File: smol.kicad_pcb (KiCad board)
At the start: 2 copper layers, 141 parts, among them SW1 keyswitch, SW10 keyswitch, SW11 keyswitch, SW12 keyswitch, SW13 keyswitch, SW14 keyswitch, SW15 keyswitch, SW16 keyswitch, SW17 keyswitch, SW18 keyswitch, SW19 keyswitch, SW2 keyswitch, SW20 keyswitch, SW21 keyswitch, SW22 keyswitch, SW23 keyswitch, SW24 keyswitch, SW25 keyswitch, SW26 keyswitch, SW27 keyswitch, SW28 keyswitch, SW29 keyswitch, SW3 keyswitch, SW30 keyswitch, SW31 keyswitch, SW32 keyswitch, SW33 keyswitch, SW34 keyswitch, SW35 keyswitch, SW36 keyswitch, SW37 keyswitch, SW38 keyswitch, SW39 keyswitch, SW4 keyswitch, SW40 keyswitch, SW41 keyswitch, SW42 keyswitch, SW43 keyswitch, SW44 keyswitch, SW45 keyswitch, SW46 keyswitch, SW47 keyswitch, SW48 keyswitch, SW49 keyswitch, SW5 keyswitch, SW50 keyswitch, SW51 keyswitch, SW52 keyswitch, SW53 keyswitch, SW54 keyswitch, SW55 keyswitch, SW56 keyswitch, SW57 keyswitch, SW58 keyswitch, SW59 keyswitch, SW6 keyswitch, SW60 keyswitch, SW61 keyswitch, SW62 keyswitch, SW63 keyswitch, SW64 keyswitch, SW65 keyswitch, SW66 keyswitch, SW67 keyswitch, SW68 keyswitch, SW69 keyswitch, SW7 keyswitch, SW70 keyswitch, SW8 keyswitch, SW9 keyswitch, U1 MiniF4x1Cx_V31

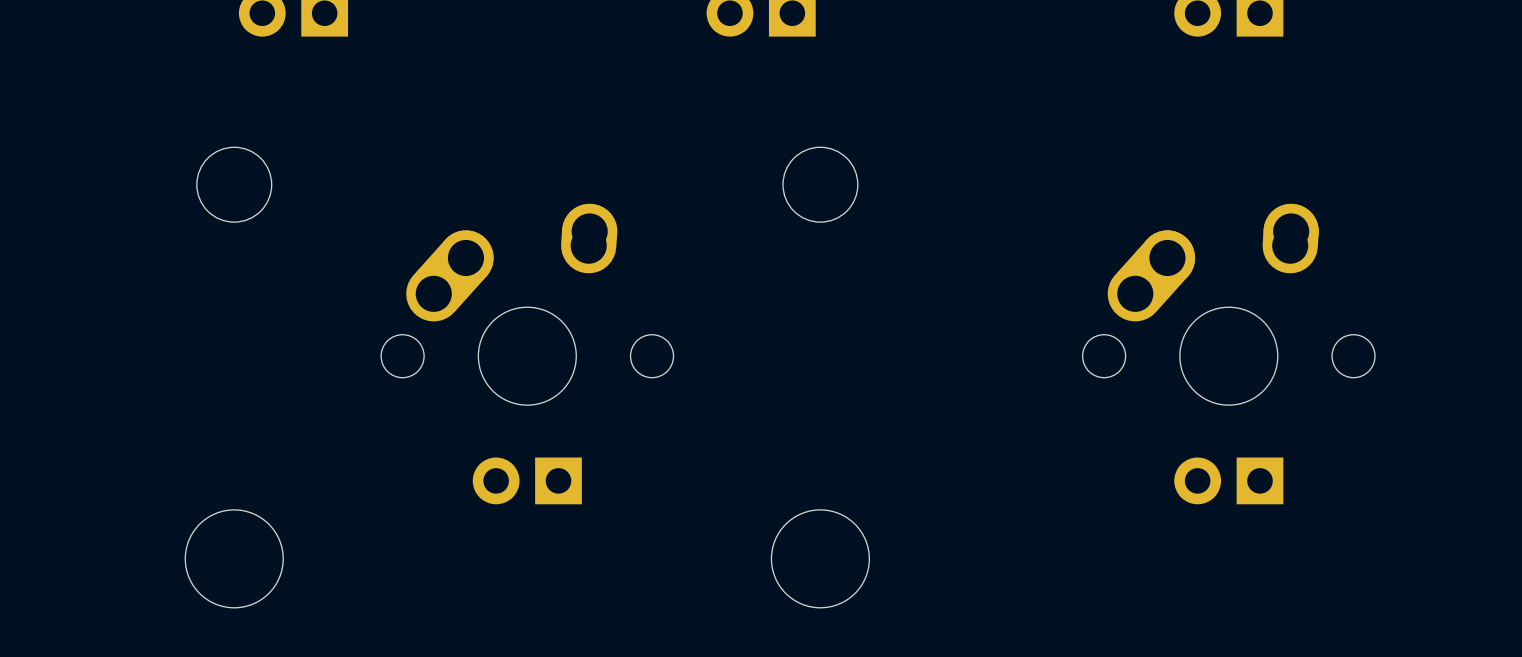
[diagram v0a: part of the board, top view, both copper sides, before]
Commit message: move space bar one key to the right
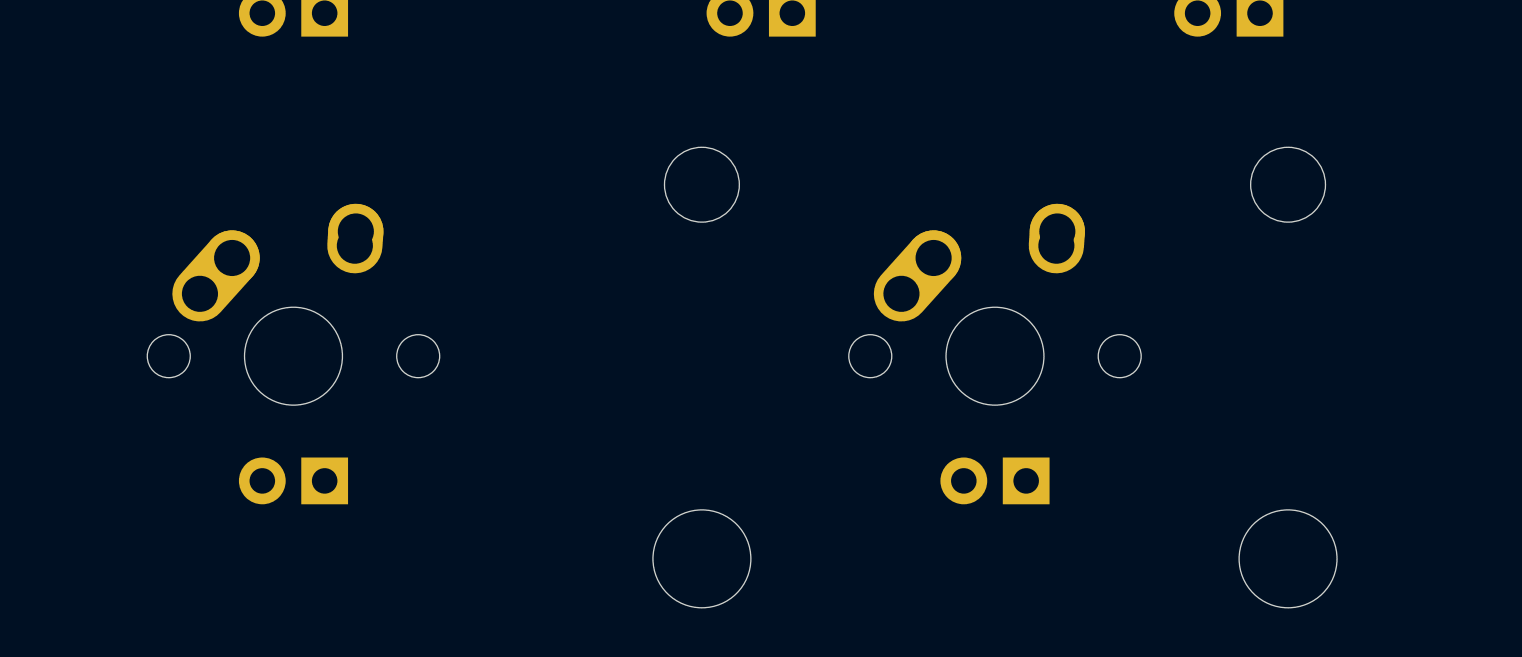
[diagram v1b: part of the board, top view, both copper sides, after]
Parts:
- SW62: footprint MX_Alps_Hybrid:MX-2U -> MX_Alps_Hybrid:MX-1U
- SW63: footprint MX_Alps_Hybrid:MX-1U -> MX_Alps_Hybrid:MX-2U
- moved SW62 9.53 mm to (110.3, 99.2)
- moved SW63 9.53 mm to (138.9, 99.2)

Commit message: position diodes on pcb
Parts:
- D1, D10, D11, D12, D13, D14, D15, D16, D17, D18, D19, D2, D20, D21, D22, D23, D24, D25, D26, D27, D28, D29, D3, D30, D31, D32, D33, D34, D35, D36, D37, D38, D39, D4, D40, D41, D42, D43, D44, D45, D46, D47, D48, D49, D5, D50, D51, D52, D53, D54, D55, D56, D57, D58, D59, D6, D60, D61, D62, D63, D64, D65, D66, D67, D68, D69, D7, D70, D8, D9: moved to B.Cu
- moved D15 436.7 mm to (22.2, 50.0), turned to 270 degrees
- moved D16 404.2 mm to (50.8, 50.0), turned to 270 degrees
- moved D57 387.4 mm to (12.7, 107.2), turned to 270 degrees
- moved D30 384.3 mm to (31.8, 69.1), turned to 270 degrees
- moved D32 381.1 mm to (69.8, 69.1), turned to 270 degrees
- moved D43 380.6 mm to (22.2, 88.1), turned to 270 degrees
- moved D1 370.5 mm to (12.7, 31.0), turned to 270 degrees
- moved D44 366.1 mm to (50.8, 88.1), turned to 270 degrees
- moved D58 365.4 mm to (31.8, 107.2), turned to 270 degrees
- moved D46 346.5 mm to (88.9, 88.1), turned to 270 degrees
- moved D59 343.6 mm to (50.8, 107.2), turned to 270 degrees
- moved D34 340.0 mm to (108.0, 69.1), turned to 270 degrees
- moved D47 324.4 mm to (108.0, 88.1), turned to 270 degrees
- moved D33 324.2 mm to (88.9, 69.1), turned to 270 degrees
- moved D60 322.1 mm to (69.8, 107.2), turned to 270 degrees
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
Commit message: switch to mx switch footprints and line up diodes
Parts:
- SW1, SW10, SW11, SW12, SW13, SW16, SW17, SW18, SW19, SW2, SW20, SW21, SW22, SW23, SW24, SW25, SW26, SW27, SW28, SW29, SW3, SW30, SW31, SW32, SW33, SW34, SW35, SW36, SW37, SW38, SW39, SW4, SW40, SW41, SW44, SW45, SW46, SW47, SW48, SW49, SW5, SW50, SW51, SW52, SW53, SW54, SW55, SW56, SW57, SW58, SW59, SW6, SW60, SW61, SW62, SW64, SW65, SW66, SW67, SW68, SW69, SW7, SW70, SW8, SW9: value keyswitch -> 1U; footprint MX_Alps_Hybrid:MX-1U -> MX_Only:MXOnly-1U-NoLED
- SW14, SW15, SW42, SW43, SW63: value keyswitch -> 2U; footprint MX_Alps_Hybrid:MX-2U -> MX_Only:MXOnly-2U-NoLED
- moved D11 4.63 mm to (205.6, 27.0), turned to 0 degrees
- moved D14 4.63 mm to (272.3, 27.0), turned to 0 degrees
- moved D24 4.63 mm to (205.6, 46.0), turned to 0 degrees
- moved D28 4.63 mm to (281.8, 46.0), turned to 0 degrees
- moved D39 4.63 mm to (205.6, 65.1), turned to 0 degrees
- moved D42 4.63 mm to (272.3, 65.1), turned to 0 degrees
- moved D52 4.63 mm to (205.6, 84.1), turned to 0 degrees
- moved D56 4.63 mm to (281.8, 84.1), turned to 0 degrees
- moved D66 4.63 mm to (205.6, 103.2), turned to 0 degrees
- moved D70 4.63 mm to (281.8, 103.2), turned to 0 degrees
- moved D17 4.63 mm to (72.2, 46.0), turned to 0 degrees
- moved D32 4.63 mm to (72.2, 65.1), turned to 0 degrees
- moved D4 4.63 mm to (72.2, 27.0), turned to 0 degrees
- moved D45 4.63 mm to (72.2, 84.1), turned to 0 degrees
- moved D60 4.63 mm to (72.2, 103.2), turned to 0 degrees
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
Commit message: connect matrix to blackpill
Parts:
- moved U1 412.2 mm to (-11.9, -15.9)
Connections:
- U1 pad 1: Net-(U1-Pad1) -> ROW5
- U1 pad 10: Net-(U1-Pad10) -> COL2
- U1 pad 11: Net-(U1-Pad11) -> COL3
- U1 pad 12: Net-(U1-Pad12) -> COL4
- U1 pad 13: Net-(U1-Pad13) -> COL5
- U1 pad 14: Net-(U1-Pad14) -> COL6
- U1 pad 15: Net-(U1-Pad15) -> COL7
- U1 pad 16: Net-(U1-Pad16) -> COL8
- U1 pad 17: Net-(U1-Pad17) -> COL9
- U1 pad 2: Net-(U1-Pad2) -> ROW4
- U1 pad 3: Net-(U1-Pad3) -> ROW3
- U1 pad 32: Net-(U1-Pad32) -> COL14
- U1 pad 33: Net-(U1-Pad33) -> COL13
- U1 pad 34: Net-(U1-Pad34) -> COL12
- U1 pad 35: Net-(U1-Pad35) -> COL11
- U1 pad 37: Net-(U1-Pad37) -> COL10
- U1 pad 4: Net-(U1-Pad4) -> ROW2
- U1 pad 5: Net-(U1-Pad5) -> ROW1
- U1 pad 7: Net-(U1-Pad7) -> COL1

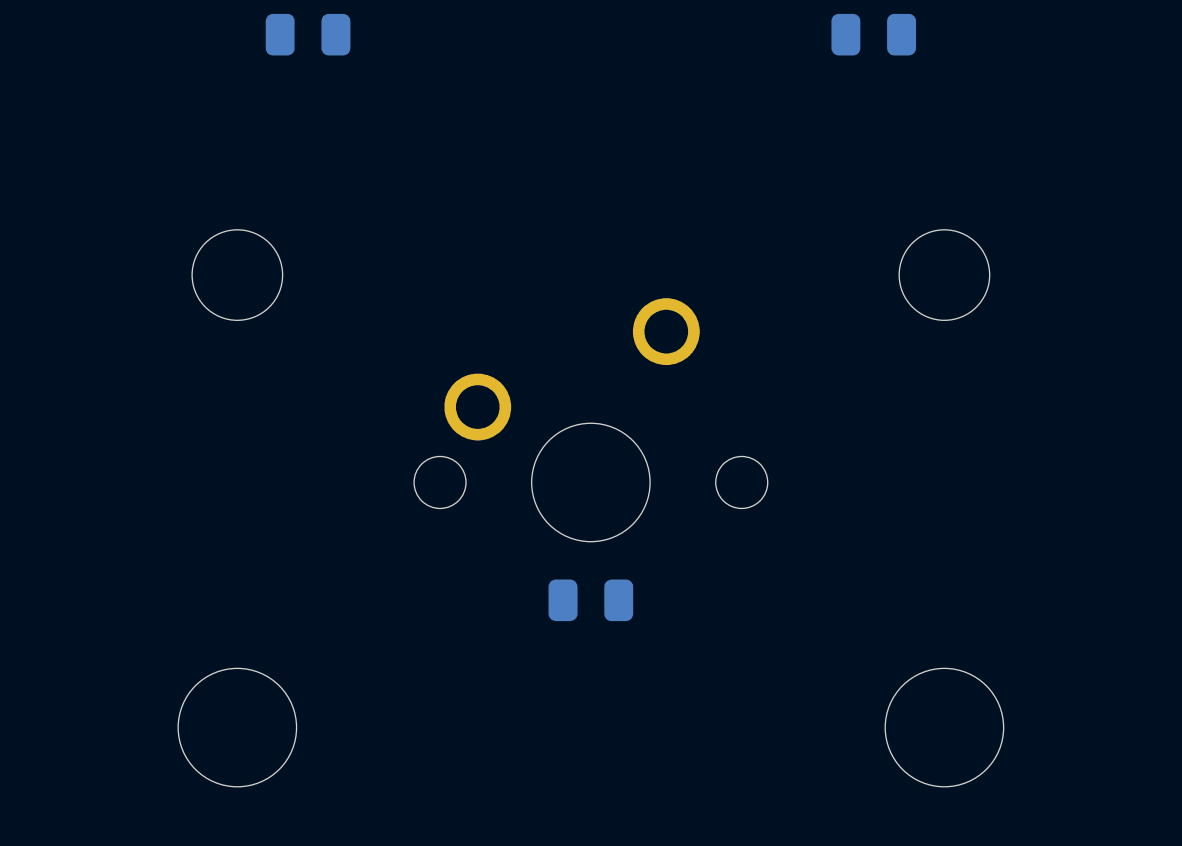
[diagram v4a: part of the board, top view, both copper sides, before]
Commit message: use inverted stab on bottow row
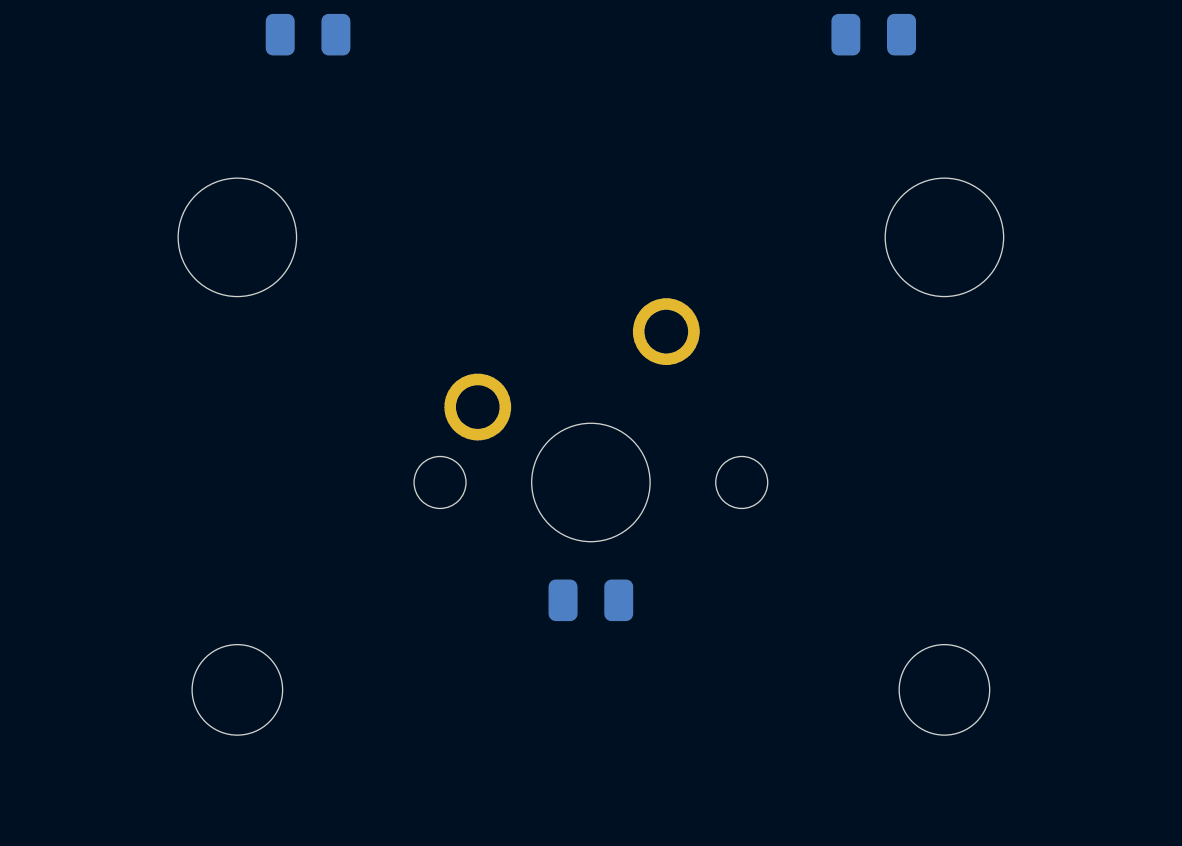
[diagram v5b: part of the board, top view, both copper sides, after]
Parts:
- SW63: footprint MX_Only:MXOnly-2U-NoLED -> MX_Only:MXOnly-2U-ReversedStabilizers-NoLED

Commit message: add leds to pcb
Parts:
- added C1: 100nf, Capacitor_SMD:C_0805_2012Metric, F.Cu at (-3.97, 23.0)
- added C10: 100nf, Capacitor_SMD:C_0805_2012Metric, F.Cu at (300.8, 23.0)
- added C2: 100nf, Capacitor_SMD:C_0805_2012Metric, F.Cu at (-3.97, 42.1)
- added C3: 100nf, Capacitor_SMD:C_0805_2012Metric, F.Cu at (-3.97, 61.1)
- added C4: 100nf, Capacitor_SMD:C_0805_2012Metric, F.Cu at (-3.97, 80.2)
- added C5: 100nf, Capacitor_SMD:C_0805_2012Metric, F.Cu at (-3.97, 99.2)
- added C6: 100nf, Capacitor_SMD:C_0805_2012Metric, F.Cu at (300.8, 99.2)
- added C7: 100nf, Capacitor_SMD:C_0805_2012Metric, F.Cu at (300.8, 80.2)
- added C8: 100nf, Capacitor_SMD:C_0805_2012Metric, F.Cu at (300.8, 61.1)
- added C9: 100nf, Capacitor_SMD:C_0805_2012Metric, F.Cu at (300.8, 42.1)
- added Q1: BSS138, Package_TO_SOT_SMD:SOT-23, F.Cu at (-10.3, -34.1)
- added R1: 10k, Resistor_SMD:R_0805_2012Metric, F.Cu at (-34.9, -34.1)
- added R2: 10k, Resistor_SMD:R_0805_2012Metric, F.Cu at (-26.2, -32.5)
- added RGB1: SK6812, LED_SMD:LED_SK6812_PLCC4_5.0x5.0mm_P3.2mm, F.Cu at (0.79, 23.0)
- added RGB10: SK6812, LED_SMD:LED_SK6812_PLCC4_5.0x5.0mm_P3.2mm, F.Cu at (296.1, 23.0)
- added RGB2: SK6812, LED_SMD:LED_SK6812_PLCC4_5.0x5.0mm_P3.2mm, F.Cu at (0.79, 42.1)
- added RGB3: SK6812, LED_SMD:LED_SK6812_PLCC4_5.0x5.0mm_P3.2mm, F.Cu at (0.79, 61.1)
- added RGB4: SK6812, LED_SMD:LED_SK6812_PLCC4_5.0x5.0mm_P3.2mm, F.Cu at (0.79, 80.2)
- added RGB5: SK6812, LED_SMD:LED_SK6812_PLCC4_5.0x5.0mm_P3.2mm, F.Cu at (0.79, 99.2)
- added RGB6: SK6812, LED_SMD:LED_SK6812_PLCC4_5.0x5.0mm_P3.2mm, F.Cu at (296.1, 99.2)
- added RGB7: SK6812, LED_SMD:LED_SK6812_PLCC4_5.0x5.0mm_P3.2mm, F.Cu at (296.1, 80.2)
- added RGB8: SK6812, LED_SMD:LED_SK6812_PLCC4_5.0x5.0mm_P3.2mm, F.Cu at (296.1, 61.1)
- added RGB9: SK6812, LED_SMD:LED_SK6812_PLCC4_5.0x5.0mm_P3.2mm, F.Cu at (296.1, 42.1)
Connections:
- net VCC renamed +3V3
- U1 pad 18: Net-(U1-Pad18) -> +5V
- U1 pad 31: Net-(U1-Pad31) -> COL14
- U1 pad 32: COL14 -> COL13
- U1 pad 33: COL13 -> COL12
- U1 pad 34: COL12 -> COL11
- U1 pad 35: COL11 -> COL10
- U1 pad 37: COL10 -> RGB
- U1 pad 40: Net-(U1-Pad40) -> +5V

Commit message: reorganize for easier routing
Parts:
- moved C1 304.8 mm to (300.8, 23.0)
- moved C10 304.8 mm to (-3.97, 23.0)
- moved C2 304.8 mm to (300.8, 42.1)
- moved C3 304.8 mm to (300.8, 61.1)
- moved C4 304.8 mm to (300.8, 80.2)
- moved C5 304.8 mm to (300.8, 99.2)
- moved C6 304.8 mm to (-3.97, 99.2)
- moved C7 304.8 mm to (-3.97, 80.2)
- moved C8 304.8 mm to (-3.97, 61.1)
- moved C9 304.8 mm to (-3.97, 42.1)
- moved RGB1 295.3 mm to (296.1, 23.0)
- moved RGB10 295.3 mm to (0.79, 23.0)
- moved RGB2 295.3 mm to (296.1, 42.1)
- moved RGB3 295.3 mm to (296.1, 61.1)
- moved RGB4 295.3 mm to (296.1, 80.2)
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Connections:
- U1 pad 31: COL14 -> COL10
- U1 pad 32: COL13 -> COL11
- U1 pad 34: COL11 -> COL13
- U1 pad 35: COL10 -> COL14

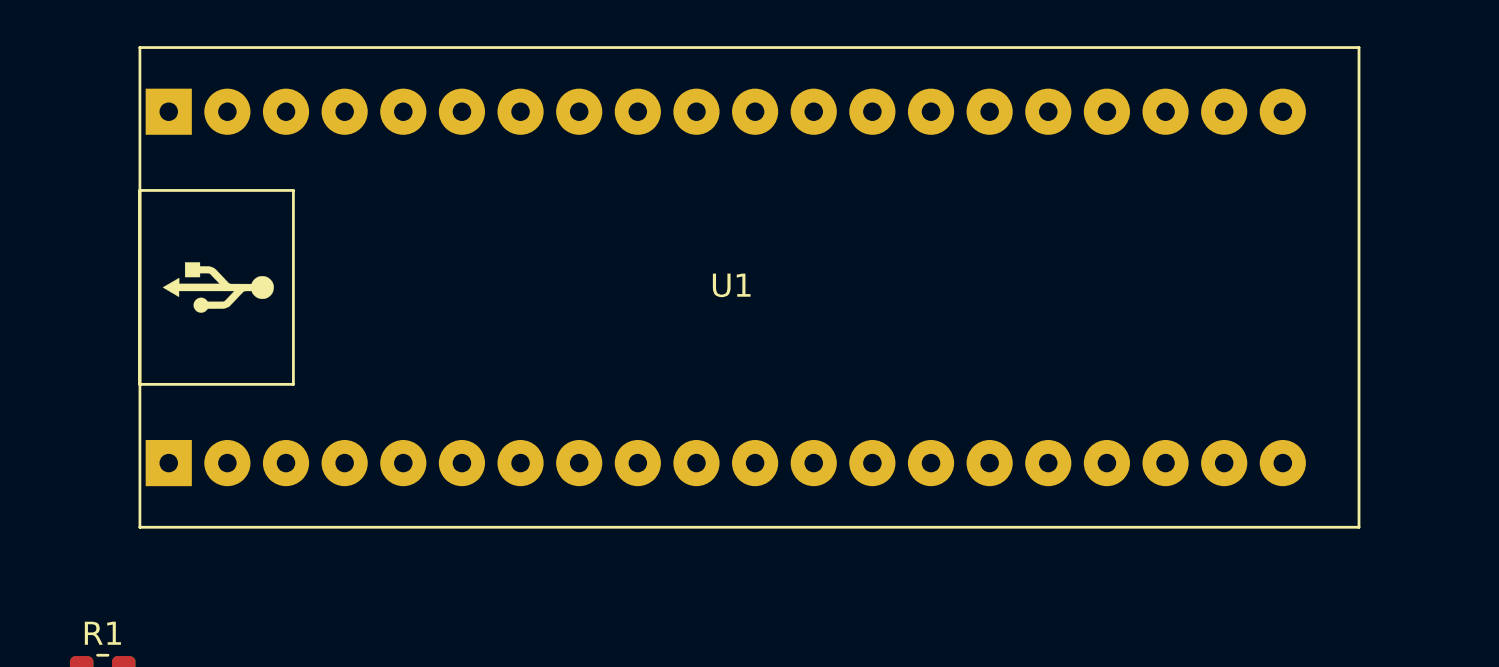
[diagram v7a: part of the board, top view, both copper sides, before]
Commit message: flip blackpill to back of pcb
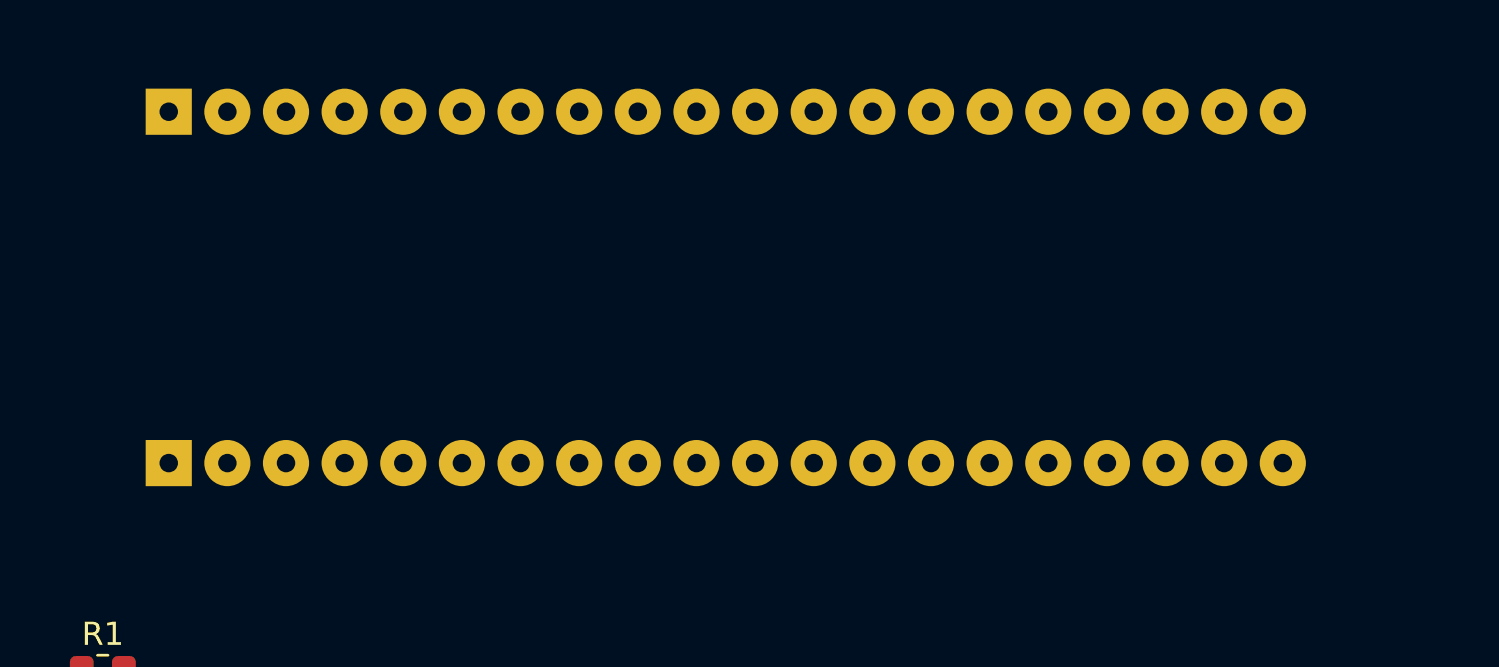
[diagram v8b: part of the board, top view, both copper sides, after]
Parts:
- U1: moved to B.Cu
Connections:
- U1 pad 1: ROW5 -> Net-(U1-Pad1)
- U1 pad 10: COL2 -> COL14
- U1 pad 11: COL3 -> COL13
- U1 pad 12: COL4 -> COL12
- U1 pad 13: COL5 -> COL11
- U1 pad 14: COL6 -> COL10
- U1 pad 15: COL7 -> COL9
- U1 pad 17: COL9 -> COL7
- U1 pad 2: ROW4 -> Net-(U1-Pad2)
- U1 pad 26: Net-(U1-Pad26) -> COL6
- U1 pad 27: Net-(U1-Pad27) -> COL5
- U1 pad 28: Net-(U1-Pad28) -> COL4
- U1 pad 29: Net-(U1-Pad29) -> COL3
- U1 pad 3: ROW3 -> Net-(U1-Pad3)
- U1 pad 30: Net-(U1-Pad30) -> COL2
- U1 pad 31: COL10 -> COL1
- U1 pad 32: COL11 -> ROW1
- U1 pad 33: COL12 -> ROW2
- U1 pad 34: COL13 -> ROW3
- U1 pad 35: COL14 -> ROW4
- U1 pad 37: RGB -> ROW5
- U1 pad 4: ROW2 -> Net-(U1-Pad4)
- U1 pad 5: ROW1 -> Net-(U1-Pad5)
- U1 pad 7: COL1 -> RGB
